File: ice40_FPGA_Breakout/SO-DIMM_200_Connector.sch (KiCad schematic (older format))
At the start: 21 parts

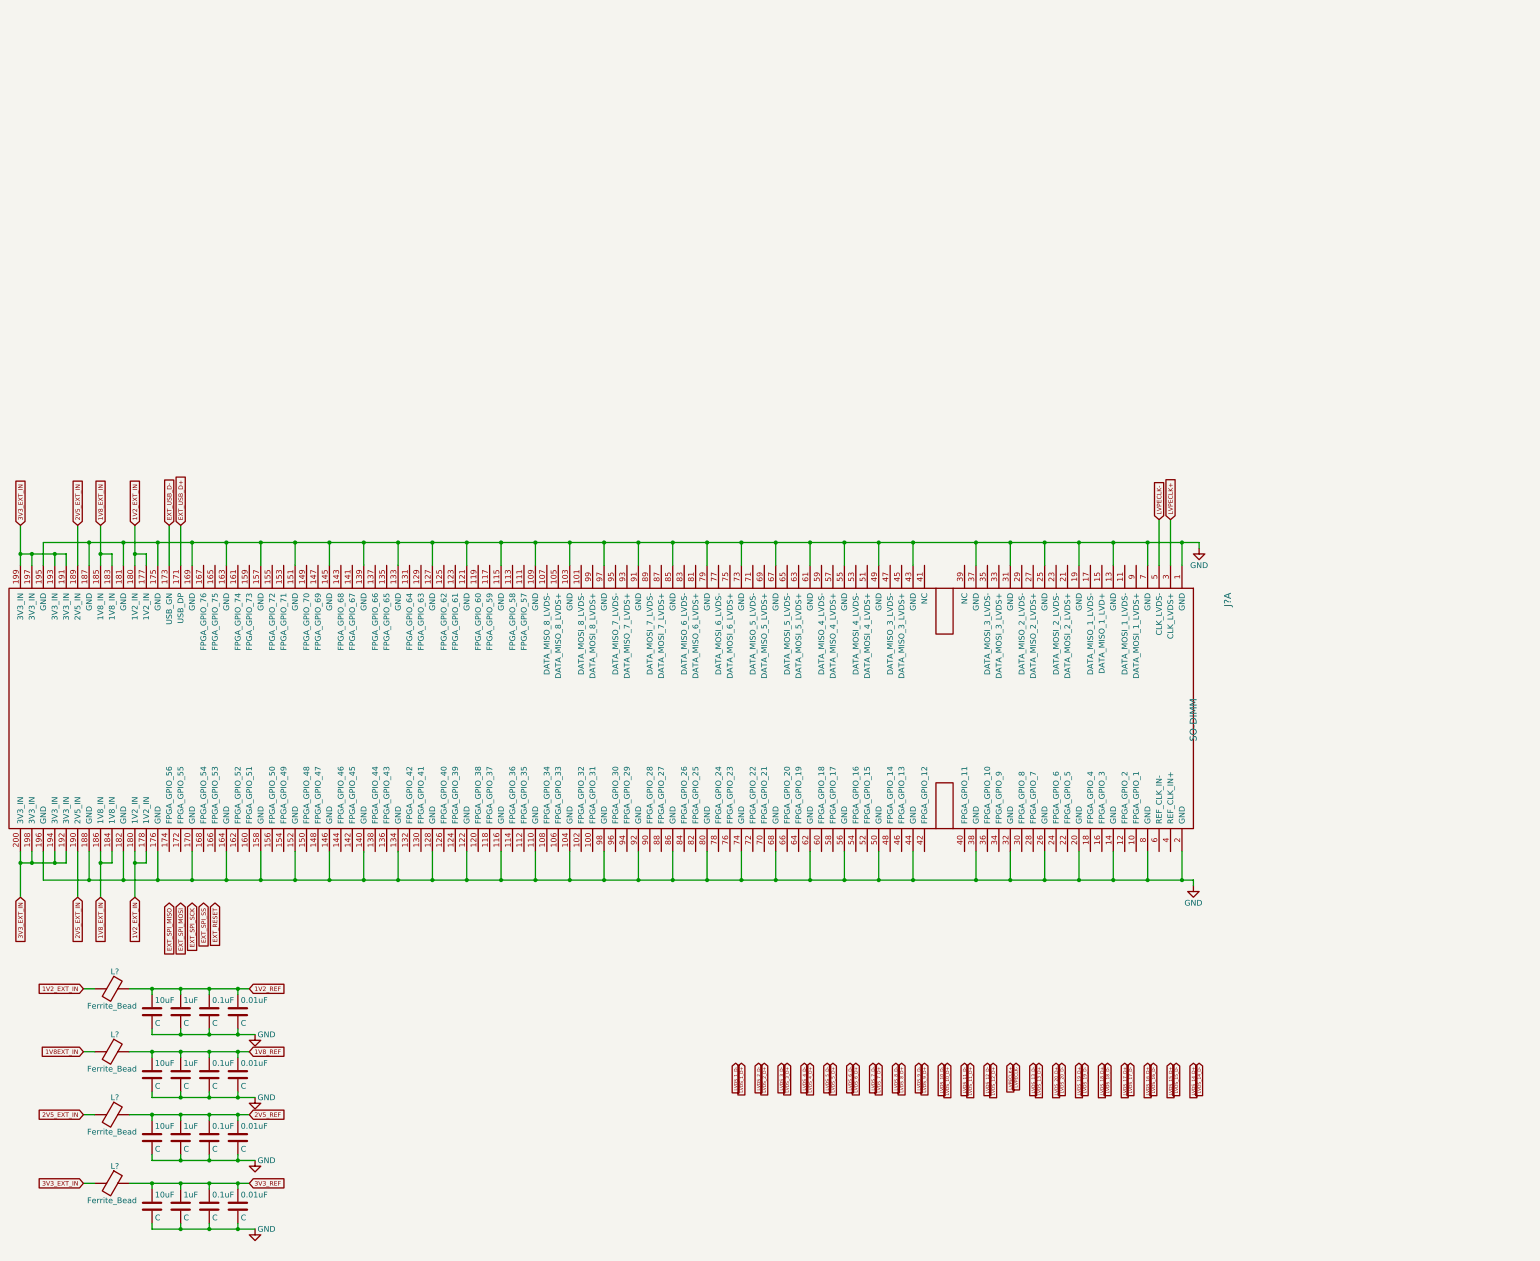
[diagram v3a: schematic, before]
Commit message: global nets changed to hierarchy net, interconnects updated
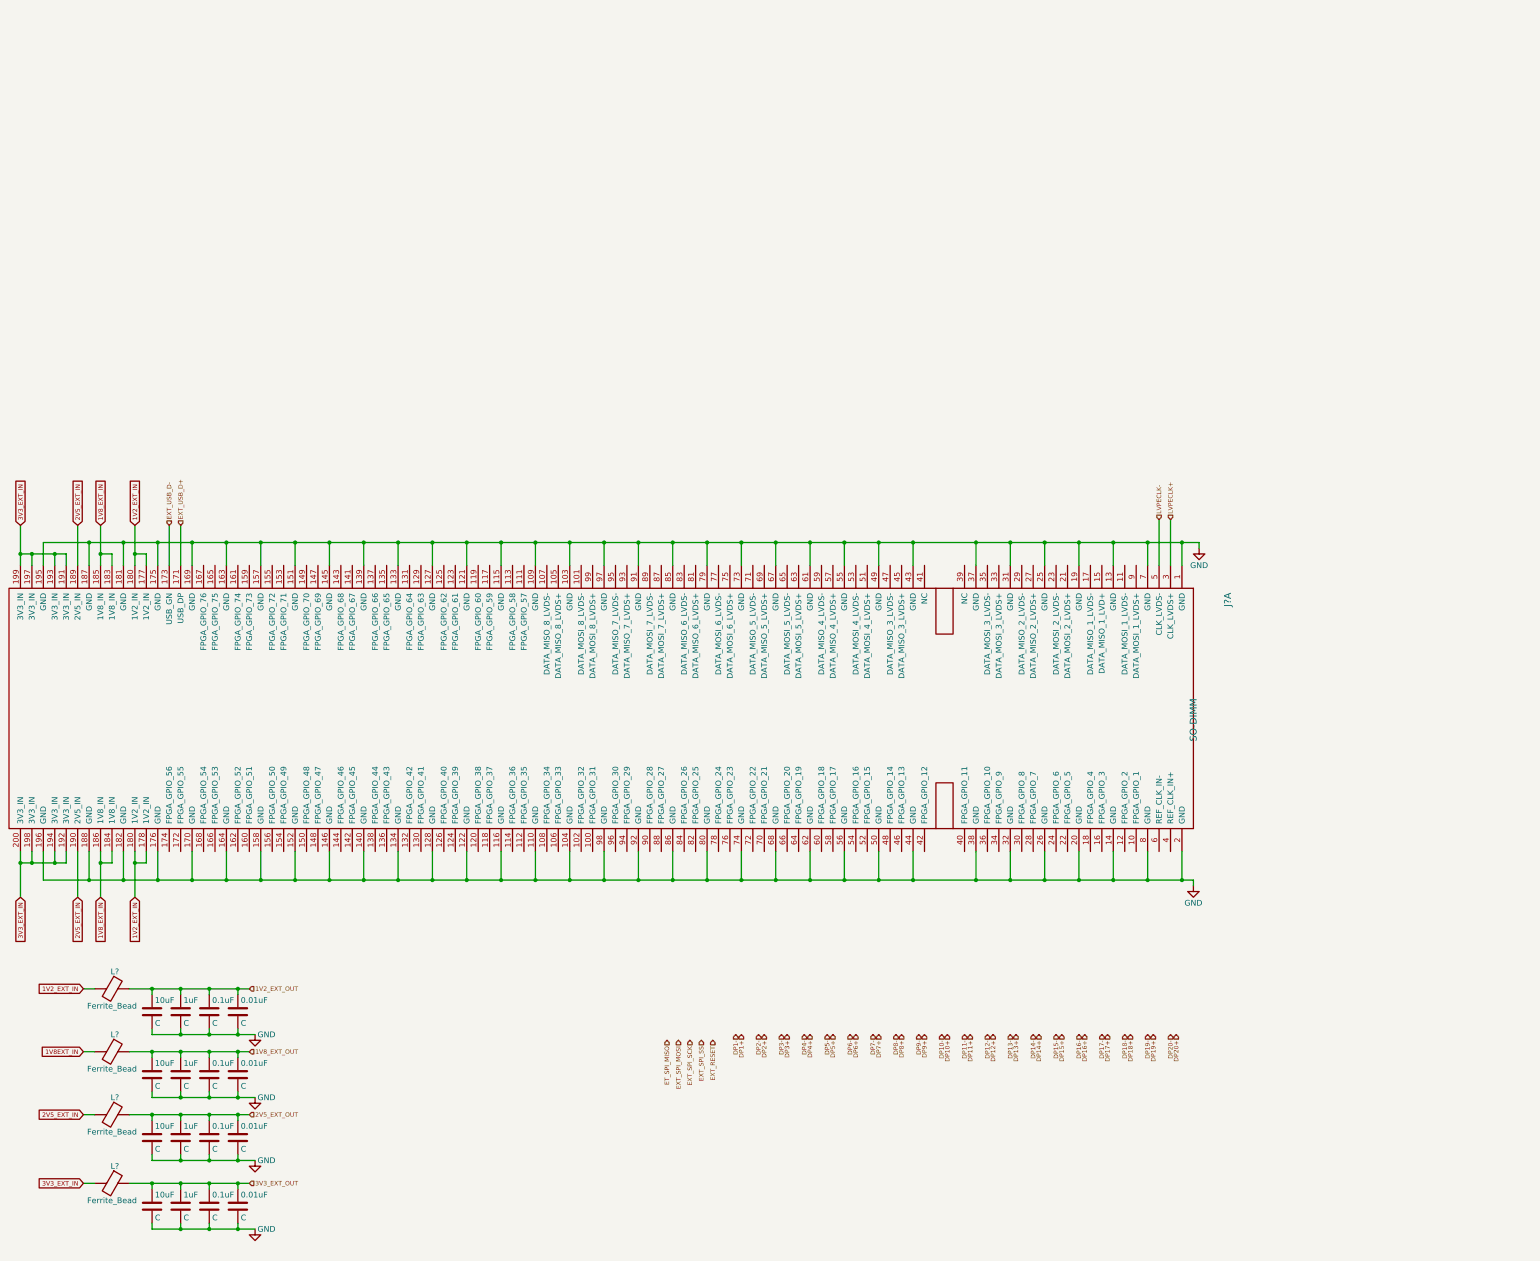
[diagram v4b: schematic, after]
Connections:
- net 1V2_REF renamed 1V2_EXT_OUT
- net 1V8_REF renamed 1V8_EXT_OUT
- net 2V5_REF renamed 2V5_EXT_OUT
- net 3V3_REF renamed 3V3_EXT_OUT
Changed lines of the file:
@@
 $Descr A4 11693 8268
 encoding utf-8
-Sheet 6 7
+Sheet 7 7
 Title ""
 Date ""
@@
 Text GLabel 1350 6500 0    39   Input ~ 0
 2V5_EXT_IN
-Text GLabel 2800 6500 2    39   Input ~ 0
-2V5_REF
-Text GLabel 2800 5950 2    39   Input ~ 0
-1V8_REF
-Text GLabel 2800 5400 2    39   Input ~ 0
-1V2_REF
-Text GLabel 2800 7100 2    39   Input ~ 0
-3V3_REF
-$Comp
-L GND #PWR?
+$Comp
+L GND #PWR038
 U 1 1 5A41B6AD
 P 2850 5800
-F 0 "#PWR?" H 2850 5550 50  0001 C CNN
+F 0 "#PWR038" H 2850 5550 50  0001 C CNN
 F 1 "GND" H 2950 5800 50  0000 C CNN
 F 2 "" H 2850 5800 50  0001 C CNN
@@
 $EndComp
 $Comp
-L GND #PWR?
+L GND #PWR039
 U 1 1 5A41B7D9
 P 2850 6350
-F 0 "#PWR?" H 2850 6100 50  0001 C CNN
+F 0 "#PWR039" H 2850 6100 50  0001 C CNN
 F 1 "GND" H 2950 6350 50  0000 C CNN
 F 2 "" H 2850 6350 50  0001 C CNN
@@
 $EndComp
 $Comp
-L GND #PWR?
+L GND #PWR040
 U 1 1 5A41B927
 P 2850 7500
-F 0 "#PWR?" H 2850 7250 50  0001 C CNN
+F 0 "#PWR040" H 2850 7250 50  0001 C CNN
 F 1 "GND" H 2950 7500 50  0000 C CNN
 F 2 "" H 2850 7500 50  0001 C CNN
@@
 $EndComp
 $Comp
-L GND #PWR?
+L GND #PWR041
 U 1 1 5A41B976
 P 2850 6900
-F 0 "#PWR?" H 2850 6650 50  0001 C CNN
+F 0 "#PWR041" H 2850 6650 50  0001 C CNN
 F 1 "GND" H 2950 6900 50  0000 C CNN
 F 2 "" H 2850 6900 50  0001 C CNN
@@
 	1    0    0    -1
 $EndComp
-Text GLabel 800  4600 3    39   Input ~ 0
-3V3_EXT_IN
-Text GLabel 1500 4600 3    39   Input ~ 0
-1V8_EXT_IN
-Text GLabel 1800 4600 3    39   Input ~ 0
-1V2_EXT_IN
-$Comp
-L GND #PWR?
+$Comp
+L GND #PWR042
 U 1 1 5A41CA24
 P 11050 4500
-F 0 "#PWR?" H 11050 4250 50  0001 C CNN
+F 0 "#PWR042" H 11050 4250 50  0001 C CNN
 F 1 "GND" H 11050 4350 50  0000 C CNN
 F 2 "" H 11050 4500 50  0001 C CNN
@@
 Connection ~ 10950 1500
 $Comp
-L GND #PWR?
+L GND #PWR043
 U 1 1 5A421824
 P 11100 1550
-F 0 "#PWR?" H 11100 1300 50  0001 C CNN
+F 0 "#PWR043" H 11100 1300 50  0001 C CNN
 F 1 "GND" H 11100 1400 50  0000 C CNN
 F 2 "" H 11100 1550 50  0001 C CNN
@@
 Wire Wire Line
 	1100 1700 1100 1600
-Text GLabel 800  1350 1    39   Input ~ 0
-3V3_EXT_IN
 Wire Wire Line
 	1000 1700 1000 1500
-Text GLabel 1300 1350 1    39   Input ~ 0
-2V5_EXT_IN
-Text GLabel 1500 1350 1    39   Input ~ 0
-1V8_EXT_IN
-Text GLabel 1800 1350 1    39   Input ~ 0
-1V2_EXT_IN
-Text GLabel 2200 1350 1    39   Input ~ 0
-EXT_USB_D+
-Text GLabel 2100 1350 1    39   Input ~ 0
-EXT_USB_D-
 Wire Wire Line
 	1000 4200 1000 4450
@@
 Wire Wire Line
 	1300 4200 1300 4600
-Text GLabel 1300 4600 3    39   Input ~ 0
-2V5_EXT_IN
 $Comp
 L Ferrite_Bead L?
@@
 Wire Wire Line
 	1350 7100 1450 7100
-Text GLabel 10750 1300 1    39   Input ~ 0
+Text HLabel 2800 7100 2    39   Input ~ 0
+3V3_EXT_OUT
+Text HLabel 2800 6500 2    39   Input ~ 0
+2V5_EXT_OUT
+Text HLabel 2800 5950 2    39   Input ~ 0
+1V8_EXT_OUT
+Text HLabel 2800 5400 2    39   Input ~ 0
+1V2_EXT_OUT
+Text HLabel 2100 1350 1    39   Input ~ 0
+EXT_USB_D-
+Text HLabel 2200 1350 1    39   Input ~ 0
+EXT_USB_D+
+Text HLabel 10750 1300 1    39   Input ~ 0
 LVPECLK-
-Text GLabel 10850 1300 1    39   Input ~ 0
+Text HLabel 10850 1300 1    39   Input ~ 0
 LVPECLK+
-Text GLabel 2100 4650 3    39   Input ~ 0
-EXT_SPI_MISO
-Text GLabel 2200 4650 3    39   Input ~ 0
+Text GLabel 1800 4600 3    39   Input ~ 0
+1V2_EXT_IN
+Text GLabel 1500 4600 3    39   Input ~ 0
+1V8_EXT_IN
+Text GLabel 1300 4600 3    39   Input ~ 0
+2V5_EXT_IN
+Text GLabel 800  4600 3    39   Input ~ 0
+3V3_EXT_IN
+Text GLabel 1800 1350 1    39   Input ~ 0
+1V2_EXT_IN
+Text GLabel 1500 1350 1    39   Input ~ 0
+1V8_EXT_IN
+Text GLabel 1300 1350 1    39   Input ~ 0
+2V5_EXT_IN
+Text GLabel 800  1350 1    39   Input ~ 0
+3V3_EXT_IN
+Text HLabel 7050 5800 3    39   Input ~ 0
+DP1-
+Text HLabel 7100 5800 3    39   Input ~ 0
+DP1+
+Text HLabel 7250 5800 3    39   Input ~ 0
+DP2-
+Text HLabel 7450 5800 3    39   Input ~ 0
+DP3-
+Text HLabel 7650 5800 3    39   Input ~ 0
+DP4-
+Text HLabel 7850 5800 3    39   Input ~ 0
+DP5-
+Text HLabel 8050 5800 3    39   Input ~ 0
+DP6-
+Text HLabel 8250 5800 3    39   Input ~ 0
+DP7-
+Text HLabel 8450 5800 3    39   Input ~ 0
+DP8-
+Text HLabel 8650 5800 3    39   Input ~ 0
+DP9-
+Text HLabel 8850 5800 3    39   Input ~ 0
+DP10-
+Text HLabel 9050 5800 3    39   Input ~ 0
+DP11-
+Text HLabel 9250 5800 3    39   Input ~ 0
+DP12-
+Text HLabel 9450 5800 3    39   Input ~ 0
+DP13-
+Text HLabel 9650 5800 3    39   Input ~ 0
+DP14-
+Text HLabel 9850 5800 3    39   Input ~ 0
+DP15-
+Text HLabel 10050 5800 3    39   Input ~ 0
+DP16-
+Text HLabel 10250 5800 3    39   Input ~ 0
+DP17-
+Text HLabel 10450 5800 3    39   Input ~ 0
+DP18-
+Text HLabel 10650 5800 3    39   Input ~ 0
+DP19-
+Text HLabel 10850 5800 3    39   Input ~ 0
+DP20-
+Text HLabel 7300 5800 3    39   Input ~ 0
+DP2+
+Text HLabel 7500 5800 3    39   Input ~ 0
+DP3+
+Text HLabel 7700 5800 3    39   Input ~ 0
+DP4+
+Text HLabel 7900 5800 3    39   Input ~ 0
+DP5+
+Text HLabel 8100 5800 3    39   Input ~ 0
+DP6+
+Text HLabel 8300 5800 3    39   Input ~ 0
+DP7+
+Text HLabel 8500 5800 3    39   Input ~ 0
+DP8+
+Text HLabel 8700 5800 3    39   Input ~ 0
+DP9+
+Text HLabel 8900 5800 3    39   Input ~ 0
+DP10+
+Text HLabel 9100 5800 3    39   Input ~ 0
+DP11+
+Text HLabel 9300 5800 3    39   Input ~ 0
+DP12+
+Text HLabel 9500 5800 3    39   Input ~ 0
+DP13+
+Text HLabel 9700 5800 3    39   Input ~ 0
+DP14+
+Text HLabel 9900 5800 3    39   Input ~ 0
+DP15+
+Text HLabel 10100 5800 3    39   Input ~ 0
+DP16+
+Text HLabel 10300 5800 3    39   Input ~ 0
+DP17+
+Text HLabel 10500 5800 3    39   Input ~ 0
+DP18+
+Text HLabel 10700 5800 3    39   Input ~ 0
+DP19+
+Text HLabel 10900 5800 3    39   Input ~ 0
+DP20+
+Text HLabel 6450 5850 3    39   Input ~ 0
+ET_SPI_MISO
+Text HLabel 6550 5850 3    39   Input ~ 0
 EXT_SPI_MOSI
-Text GLabel 2400 4650 3    39   Input ~ 0
+Text HLabel 6650 5850 3    39   Input ~ 0
+EXT_SPI_SCK
+Text HLabel 6750 5850 3    39   Input ~ 0
 EXT_SPI_SS
-Text GLabel 2300 4650 3    39   Input ~ 0
-EXT_SPI_SCK
-Text GLabel 2500 4650 3    39   Input ~ 0
+Text HLabel 6850 5850 3    39   Input ~ 0
 EXT_RESET
-Text GLabel 7050 6050 3    28   Input ~ 0
-LVDS_1_D-
-Text GLabel 7100 6050 3    28   Input ~ 0
-LVDS_1_D+
-Text GLabel 7250 6050 3    28   Input ~ 0
-LVDS_2_D-
-Text GLabel 7450 6050 3    28   Input ~ 0
-LVDS_3_D-
-Text GLabel 7650 6050 3    28   Input ~ 0
-LVDS_4_D-
-Text GLabel 7850 6050 3    28   Input ~ 0
-LVDS_5_D-
-Text GLabel 8050 6050 3    28   Input ~ 0
-LVDS_6_D-
-Text GLabel 8250 6050 3    28   Input ~ 0
-LVDS_7_D-
-Text GLabel 8450 6050 3    28   Input ~ 0
-LVDS_8_D-
-Text GLabel 8650 6050 3    28   Input ~ 0
-LVDS_9_D-
-Text GLabel 8850 6050 3    28   Input ~ 0
-LVDS_10_D-
-Text GLabel 9050 6050 3    28   Input ~ 0
-LVDS_11_D-
-Text GLabel 9250 6050 3    28   Input ~ 0
-LVDS_12_D-
-Text GLabel 9300 6050 3    28   Input ~ 0
-LVDS_12_D+
-Text GLabel 9100 6050 3    28   Input ~ 0
-LVDS_11_D+
-Text GLabel 8900 6050 3    28   Input ~ 0
-LVDS_10_D+
-Text GLabel 8700 6050 3    28   Input ~ 0
-LVDS_9_D+
-Text GLabel 8500 6050 3    28   Input ~ 0
-LVDS_8_D+
-Text GLabel 8300 6050 3    28   Input ~ 0
-LVDS_7_D+
-Text GLabel 8100 6050 3    28   Input ~ 0
-LVDS_6_D+
-Text GLabel 7900 6050 3    28   Input ~ 0
-LVDS_5_D+
-Text GLabel 7700 6050 3    28   Input ~ 0
-LVDS_4_D+
-Text GLabel 7500 6050 3    28   Input ~ 0
-LVDS_3_D+
-Text GLabel 7300 6050 3    28   Input ~ 0
-LVDS_2_D+
-Text GLabel 9650 6050 3    28   Input ~ 0
-LVDS_13_D-
-Text GLabel 9700 6050 3    28   Input ~ 0
-LVDS_13_D+
-Text GLabel 9450 6050 3    28   Input ~ 0
-LVPECLK+
-Text GLabel 9500 6050 3    28   Input ~ 0
-LVPECLK-
-Text GLabel 11100 6050 3    28   Input ~ 0
-LVDS_14_D-
-Text GLabel 10900 6050 3    28   Input ~ 0
-LVDS_15_D-
-Text GLabel 10700 6050 3    28   Input ~ 0
-LVDS_16_D-
-Text GLabel 10500 6050 3    28   Input ~ 0
-LVDS_17_D-
-Text GLabel 10300 6050 3    28   Input ~ 0
-LVDS_18_D-
-Text GLabel 10100 6050 3    28   Input ~ 0
-LVDS_19_D-
-Text GLabel 10050 6050 3    28   Input ~ 0
-LVDS_19_D+
-Text GLabel 9900 6050 3    28   Input ~ 0
-LVDS_20_D-
-Text GLabel 9850 6050 3    28   Input ~ 0
-LVDS_20_D+
-Text GLabel 11050 6050 3    28   Input ~ 0
-LVDS_14_D+
-Text GLabel 10850 6050 3    28   Input ~ 0
-LVDS_15_D+
-Text GLabel 10650 6050 3    28   Input ~ 0
-LVDS_16_D+
-Text GLabel 10450 6050 3    28   Input ~ 0
-LVDS_17_D+
-Text GLabel 10250 6050 3    28   Input ~ 0
-LVDS_18_D+
 $EndSCHEMATC
